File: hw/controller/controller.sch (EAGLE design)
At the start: 102 parts, among them J1 XT30XT30PW_MALE, J2 XT30XT30PW_MALE, M1 MOUNT, M2 MOUNT, M3 MOUNT, M4 MOUNT, Q1 TPH1R204PLSOP_ADVANCE_8, Q2 TPH1R204PLSOP_ADVANCE_8, Q3 TPH1R204PLSOP_ADVANCE_8, Q4 TPH1R204PLSOP_ADVANCE_8, Q5 TPH1R204PLSOP_ADVANCE_8, Q6 TPH1R204PLSOP_ADVANCE_8, U1 STM32G474CEU6, U2 TCAN334G, U3 AS5147, U4 DRV8323RS

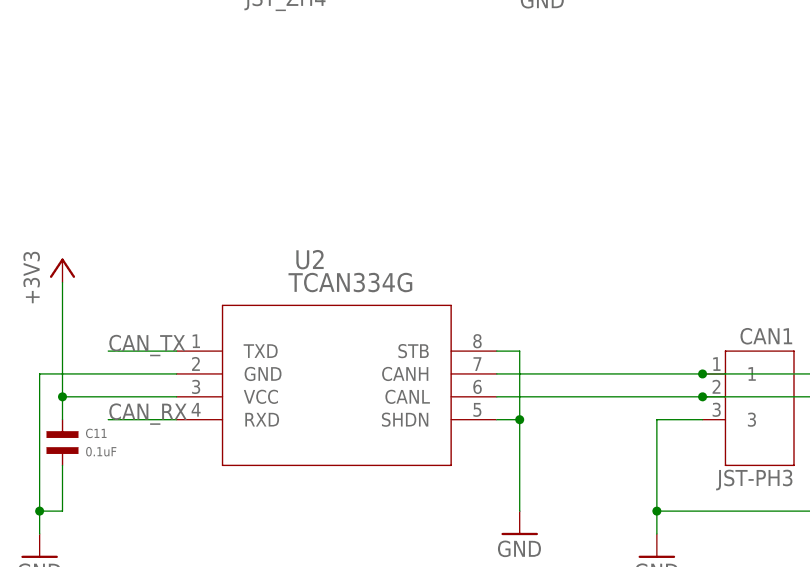
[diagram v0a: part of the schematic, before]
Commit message: Switch to actually using the SOT23-8 variant of the TCAN334G
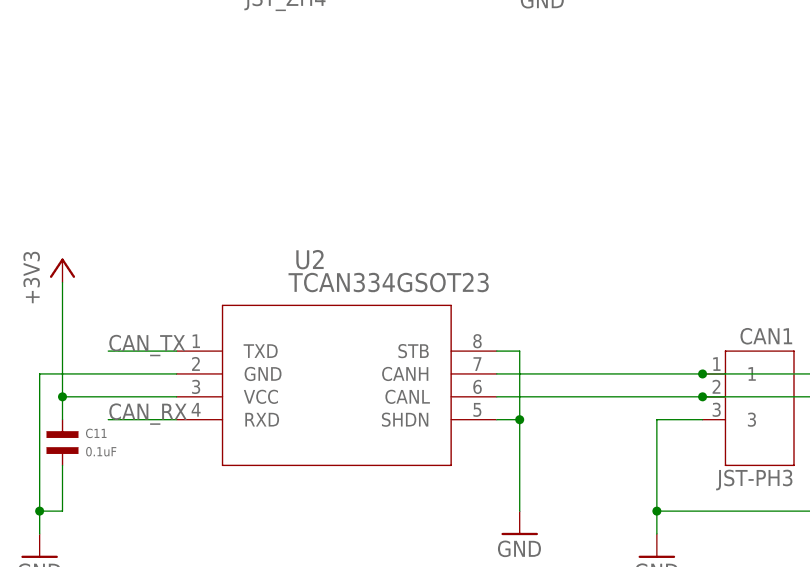
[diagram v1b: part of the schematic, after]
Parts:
- U2: value TCAN334G -> TCAN334GSOT23; device controller:TCAN334G -> controller:TCAN334GSOT23
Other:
- note added: "moteus r4 (c) jjp@pobox.com 2019 Licensed under the Apache 2.0 License"
- note removed: "moteus r4 (c) jjp@pobox.com 2019"
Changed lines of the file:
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@@
 </part>
 <part name="GND6" library="supply1" deviceset="GND" device=""/>
-<part name="U2" library="controller" deviceset="TCAN334G" device="">
+<part name="U2" library="controller" deviceset="TCAN334G" device="SOT23" value="TCAN334GSOT23">
 <attribute name="MF" value="TI"/>
 <attribute name="MPN" value="TCAN334GDCNT"/>
@@
 <text x="-132.08" y="-142.24" size="5.08" layer="90">POWER FETS</text>
 <text x="73.66" y="-142.24" size="5.08" layer="90">BULK CAPACITANCE</text>
-<text x="137.16" y="203.2" size="7.62" layer="90">moteus r4
-(c) jjp@pobox.com
-2019</text>
+<text x="-307.34" y="200.66" size="7.62" layer="90">moteus r4
+(c) jjp@pobox.com 2019
+Licensed under the Apache 2.0 License</text>
 </plain>
 <instances>

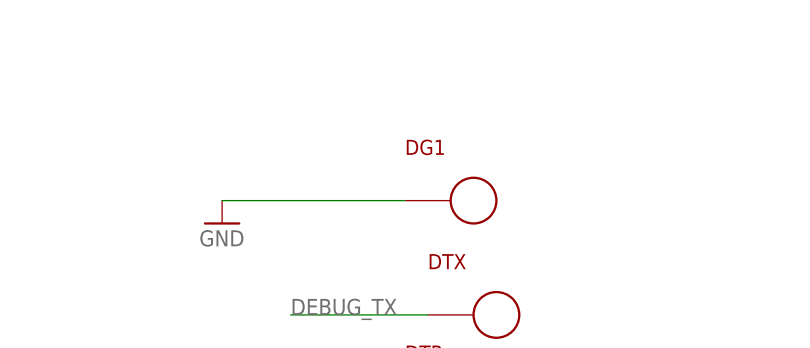
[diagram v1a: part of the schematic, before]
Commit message: Clean up outer boundary and add a 3v3 test point
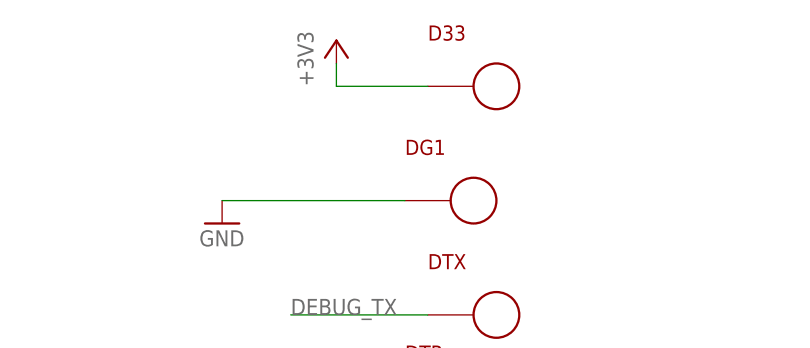
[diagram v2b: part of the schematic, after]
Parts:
- added D33: PAD24AWG_PAD, controller:PAD24AWG_PAD
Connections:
- net +3V3: now also D33.P$1
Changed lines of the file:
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@@
 <part name="GND20" library="supply1" deviceset="GND" device=""/>
 <part name="GND21" library="supply1" deviceset="GND" device=""/>
+<part name="D33" library="controller" deviceset="PAD" device="24AWG_PAD">
+<attribute name="POPULATE" value="0"/>
+</part>
+<part name="+3V13" library="supply1" deviceset="+3V3" device=""/>
 </parts>
 <sheets>
@@
 <instance part="GND20" gate="1" x="144.78" y="170.18"/>
 <instance part="GND21" gate="1" x="149.86" y="38.1"/>
+<instance part="D33" gate="G$1" x="175.26" y="185.42">
+<attribute name="POPULATE" x="175.26" y="185.42" size="7.62" layer="96" display="off"/>
+</instance>
+<instance part="+3V13" gate="G$1" x="157.48" y="190.5"/>
 </instances>
 <busses>
@@
 <wire x1="-236.22" y1="-10.16" x2="-228.6" y2="-10.16" width="0.1524" layer="91"/>
 <junction x="-228.6" y="-10.16"/>
+</segment>
+<segment>
+<pinref part="+3V13" gate="G$1" pin="+3V3"/>
+<wire x1="157.48" y1="187.96" x2="157.48" y2="185.42" width="0.1524" layer="91"/>
+<pinref part="D33" gate="G$1" pin="P$1"/>
+<wire x1="157.48" y1="185.42" x2="167.64" y2="185.42" width="0.1524" layer="91"/>
 </segment>
 </net>
@@
 </sheet>
 </sheets>
-<errors>
-</errors>
 </schematic>
 </drawing>

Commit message: Mark some more things as not populated
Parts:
- DA, DB, DC, TEMP1, TEMP2: POPULATE (none) -> 0
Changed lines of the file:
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@@
 <attribute name="MPN" value="MF-CAP-0402-0.1uF"/>
 </part>
-<part name="TEMP1" library="controller" deviceset="PAD" device="24AWG_PAD"/>
-<part name="TEMP2" library="controller" deviceset="PAD" device="24AWG_PAD"/>
-<part name="DA" library="controller" deviceset="PAD" device="24AWG_PAD"/>
-<part name="DB" library="controller" deviceset="PAD" device="24AWG_PAD"/>
-<part name="DC" library="controller" deviceset="PAD" device="24AWG_PAD"/>
+<part name="TEMP1" library="controller" deviceset="PAD" device="24AWG_PAD">
+<attribute name="POPULATE" value="0"/>
+</part>
+<part name="TEMP2" library="controller" deviceset="PAD" device="24AWG_PAD">
+<attribute name="POPULATE" value="0"/>
+</part>
+<part name="DA" library="controller" deviceset="PAD" device="24AWG_PAD">
+<attribute name="POPULATE" value="0"/>
+</part>
+<part name="DB" library="controller" deviceset="PAD" device="24AWG_PAD">
+<attribute name="POPULATE" value="0"/>
+</part>
+<part name="DC" library="controller" deviceset="PAD" device="24AWG_PAD">
+<attribute name="POPULATE" value="0"/>
+</part>
 <part name="U1" library="controller" deviceset="STM32G474CEU6" device="">
 <attribute name="MPN" value="STM32G474CEU6"/>
@@
 <attribute name="MF" x="238.76" y="-104.14" size="1.778" layer="96" display="off"/>
 </instance>
-<instance part="TEMP1" gate="G$1" x="185.42" y="-15.24"/>
-<instance part="TEMP2" gate="G$1" x="195.58" y="-17.78"/>
-<instance part="DA" gate="G$1" x="-66.04" y="-208.28" rot="R180"/>
-<instance part="DB" gate="G$1" x="-35.56" y="-208.28" rot="R180"/>
-<instance part="DC" gate="G$1" x="-10.16" y="-208.28" rot="R180"/>
+<instance part="TEMP1" gate="G$1" x="185.42" y="-15.24">
+<attribute name="POPULATE" x="185.42" y="-15.24" size="1.778" layer="96" display="off"/>
+</instance>
+<instance part="TEMP2" gate="G$1" x="195.58" y="-17.78">
+<attribute name="POPULATE" x="195.58" y="-17.78" size="1.778" layer="96" display="off"/>
+</instance>
+<instance part="DA" gate="G$1" x="-66.04" y="-208.28" rot="R180">
+<attribute name="POPULATE" x="-66.04" y="-208.28" size="1.778" layer="96" rot="R180" display="off"/>
+</instance>
+<instance part="DB" gate="G$1" x="-35.56" y="-208.28" rot="R180">
+<attribute name="POPULATE" x="-35.56" y="-208.28" size="1.778" layer="96" rot="R180" display="off"/>
+</instance>
+<instance part="DC" gate="G$1" x="-10.16" y="-208.28" rot="R180">
+<attribute name="POPULATE" x="-10.16" y="-208.28" size="1.778" layer="96" rot="R180" display="off"/>
+</instance>
 <instance part="U1" gate="G$1" x="-68.58" y="121.92">
 <attribute name="MPN" x="-68.58" y="121.92" size="7.62" layer="96" display="off"/>

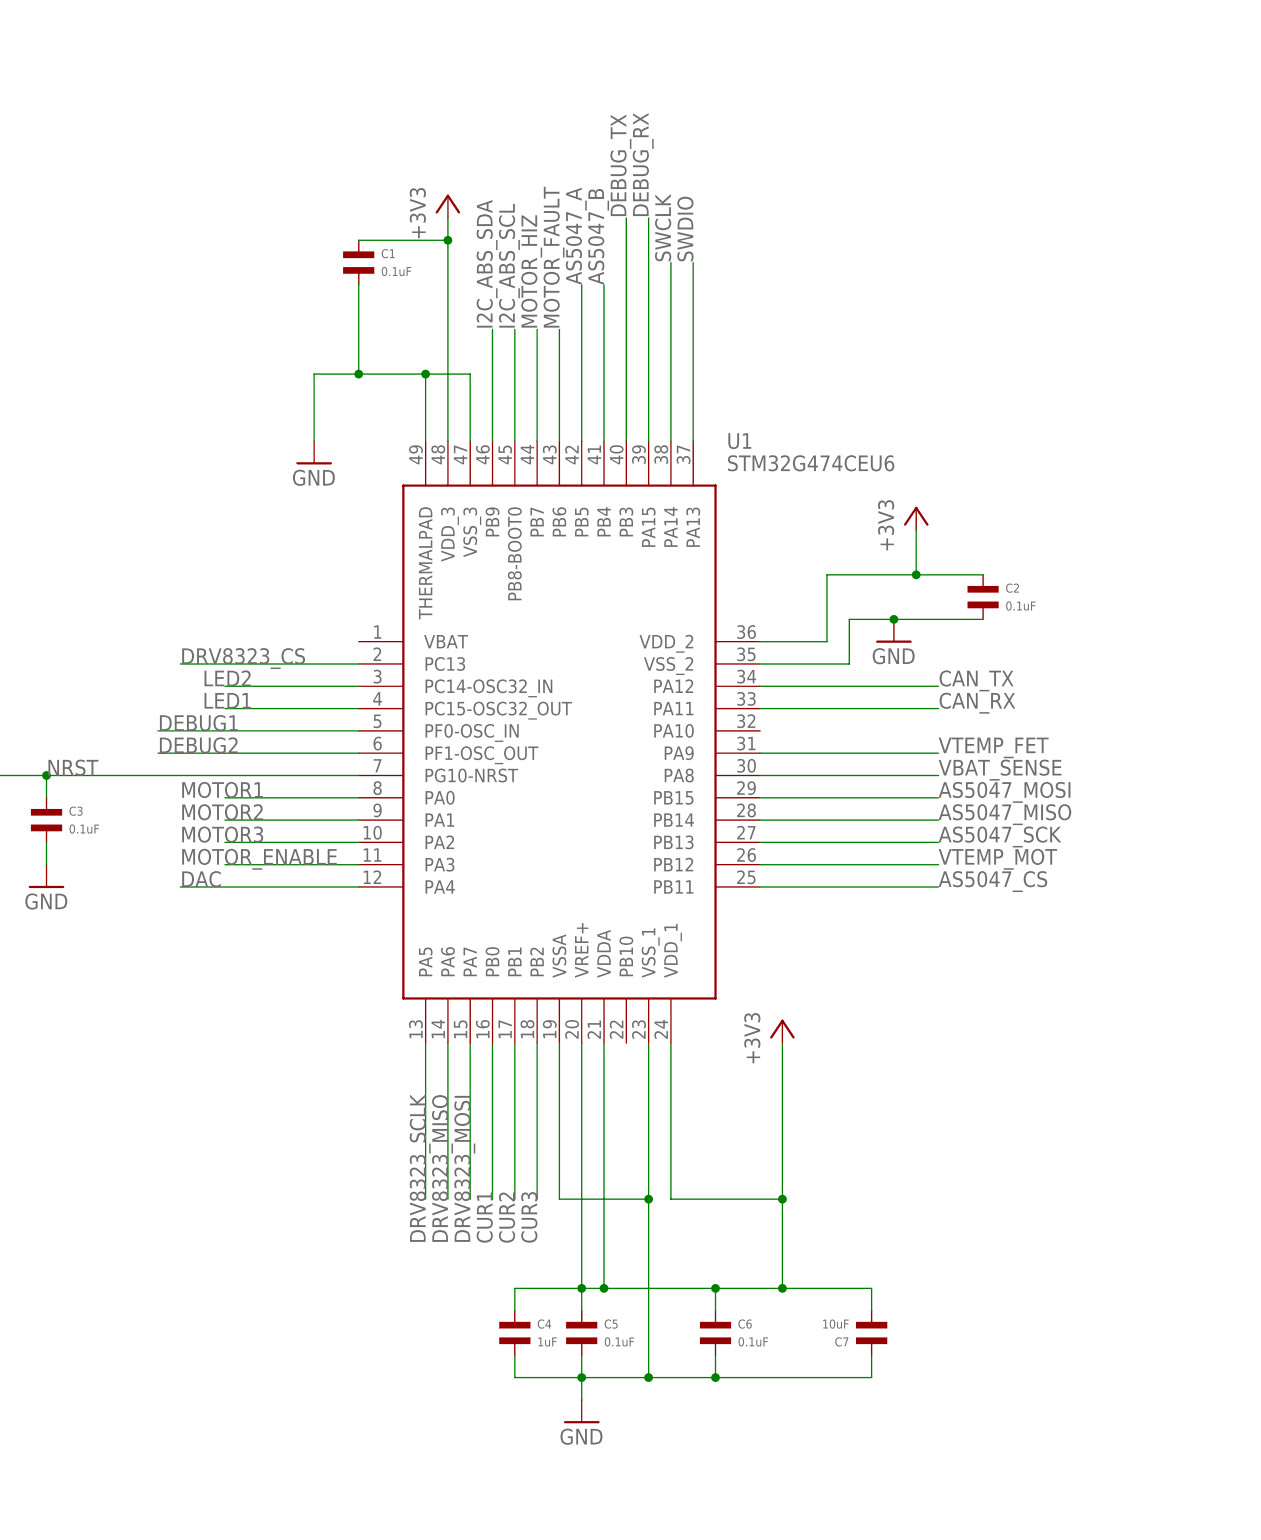
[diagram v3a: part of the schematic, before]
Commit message: controller: Likely finished r4.1 design
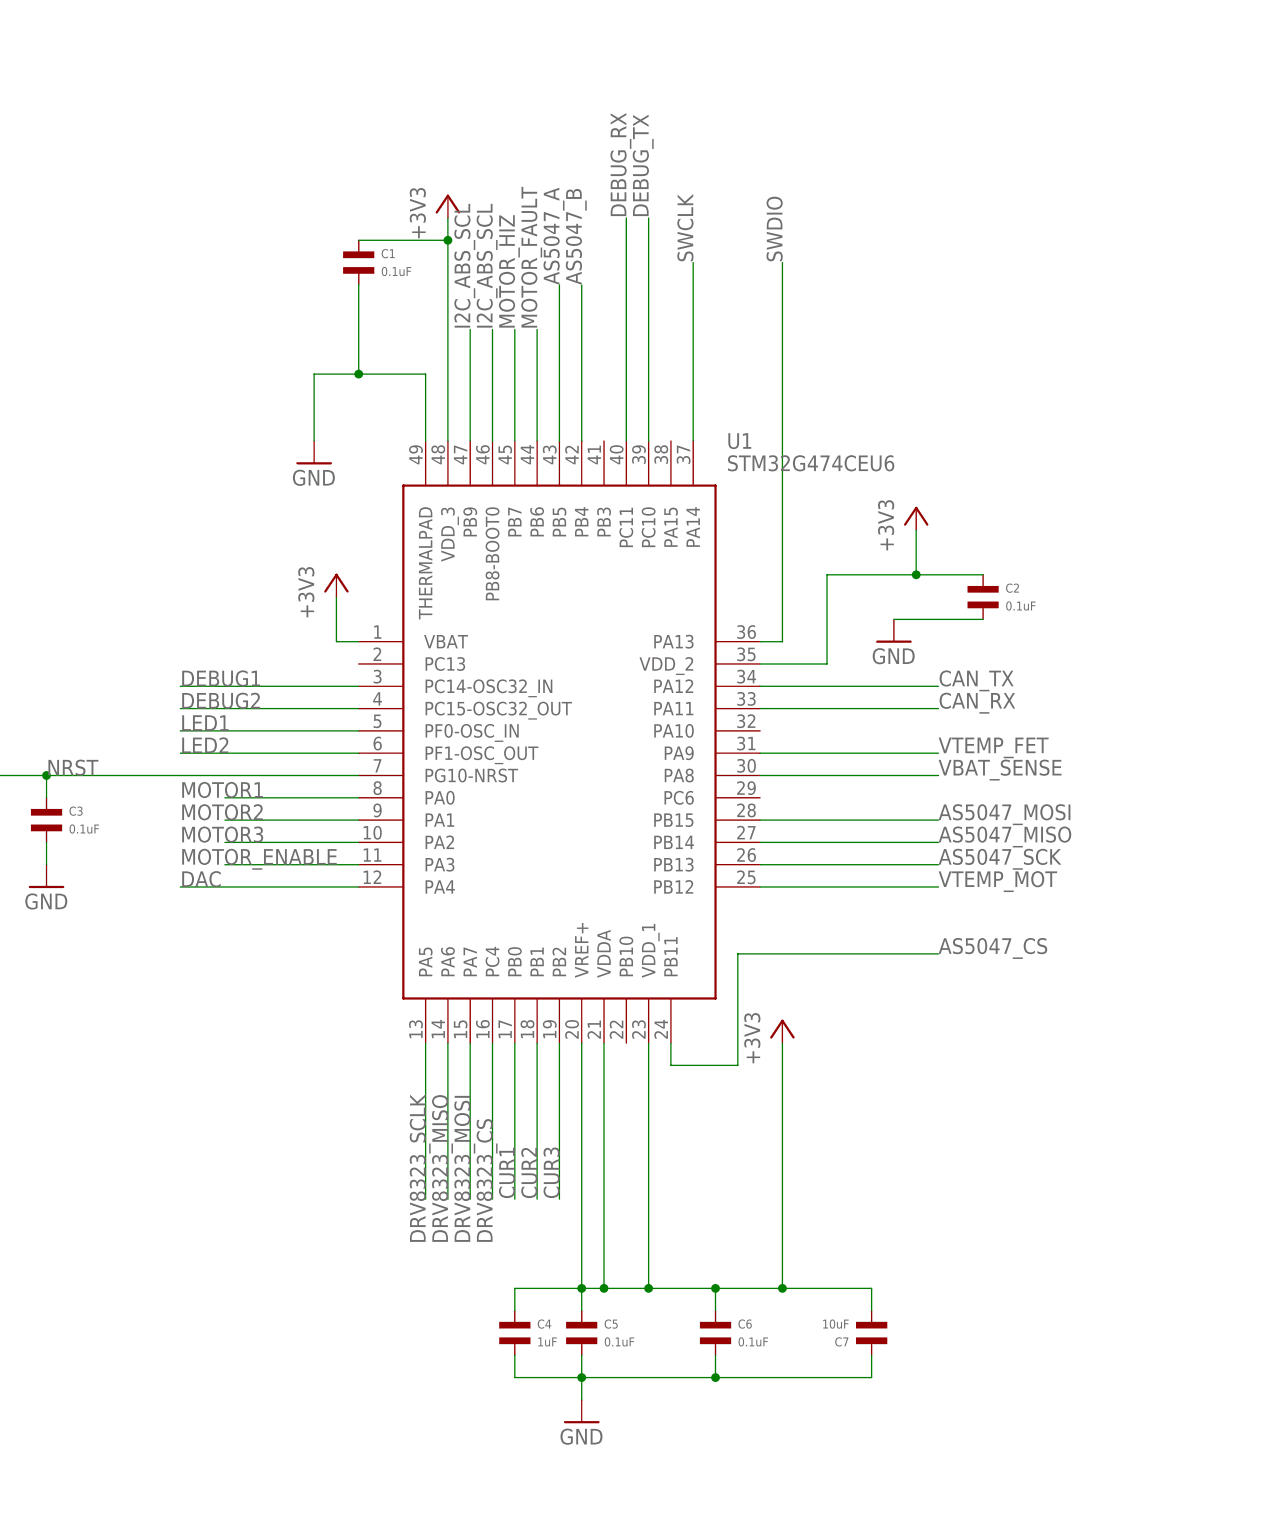
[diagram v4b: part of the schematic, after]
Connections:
- net +3V3: now also U1.VBAT
- net DEBUG1: now also U1.PC14-OSC32_IN; no longer U1.PF0-OSC_IN
- net DEBUG2: now also U1.PC15-OSC32_OUT; no longer U1.PF1-OSC_OUT
- net DEBUG_RX: now also U1.PC11; no longer U1.PA15
- net DEBUG_TX: now also U1.PC10; no longer U1.PB3
- net DRV8323_CS: now also U1.PC4; no longer U1.PC13
- net GND: no longer U1.VSSA, U1.VSS_1, U1.VSS_2, U1.VSS_3
- net I2C_ABS_SCL: now also U1.PB9
- net I2C_ABS_SDA: no longer U1.PB9
- net LED1: now also U1.PF0-OSC_IN; no longer U1.PC15-OSC32_OUT
- net LED2: now also U1.PF1-OSC_OUT; no longer U1.PC14-OSC32_IN
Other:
- note added: "moteus r4.1 (c) jjp@pobox.com 2019 Licensed under the Apache 2.0 License"
- note removed: "moteus r4 (c) jjp@pobox.com 2019 Licensed under the Apache 2.0 License"

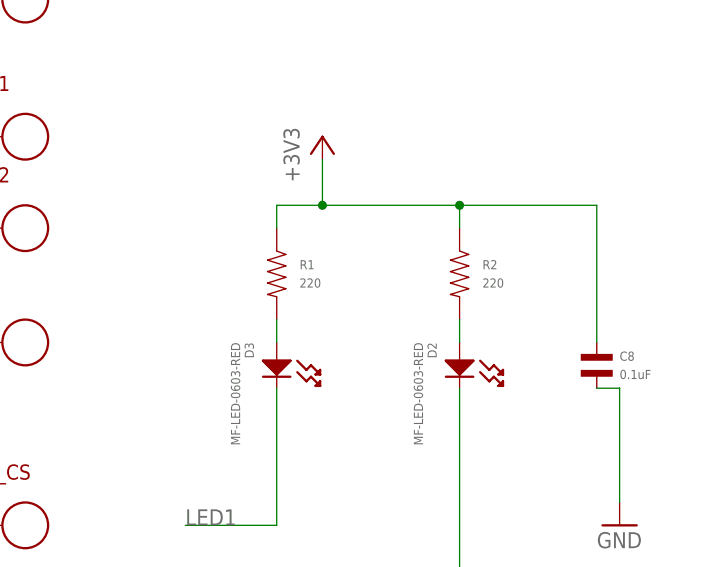
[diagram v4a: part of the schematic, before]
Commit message: controller: Switch LED resistor to 560 ohm
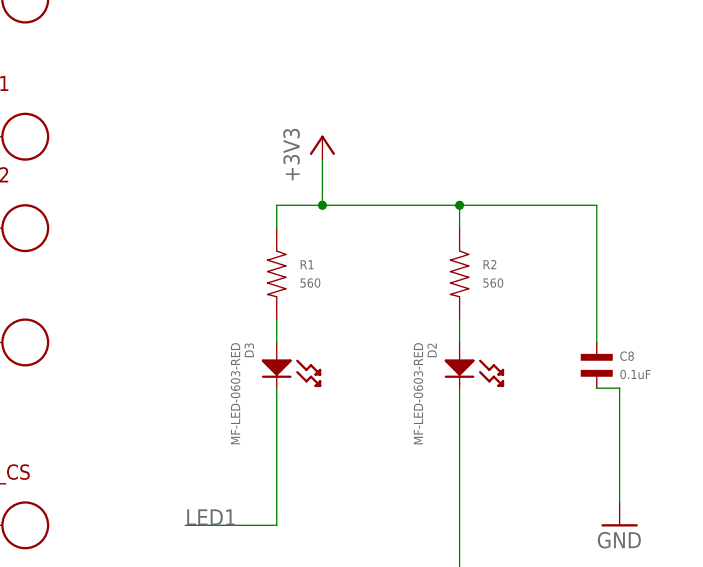
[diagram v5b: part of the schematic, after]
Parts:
- R1, R2: value 220 -> 560; MPN MF-RES-0402-220 -> MF-RES-0402-560
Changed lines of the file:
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@@
 <part name="D3" library="mfleds" deviceset="LED_SINGLE" device="-0603-RED" value="MF-LED-0603-RED"/>
 <part name="+3V7" library="supply1" deviceset="+3V3" device=""/>
-<part name="R1" library="mfpassives" deviceset="RESISTOR" device="_0402" value="220">
+<part name="R1" library="mfpassives" deviceset="RESISTOR" device="_0402" value="560">
 <attribute name="HOUSEPART" value="1"/>
-<attribute name="MPN" value="MF-RES-0402-220"/>
+<attribute name="MPN" value="MF-RES-0402-560"/>
 </part>
-<part name="R2" library="mfpassives" deviceset="RESISTOR" device="_0402" value="220">
+<part name="R2" library="mfpassives" deviceset="RESISTOR" device="_0402" value="560">
 <attribute name="HOUSEPART" value="1"/>
-<attribute name="MPN" value="MF-RES-0402-220"/>
+<attribute name="MPN" value="MF-RES-0402-560"/>
 </part>
 <part name="P+4" library="supply1" deviceset="V+" device=""/>

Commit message: controller: Actually use a 2k resistor for I2C pullup
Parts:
- R3, R4: HOUSEPART (none) -> YES; MF Panasonic -> (none); MPN ERJ-2RKF1002X -> MF-RES-0402-2K
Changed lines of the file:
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@@
 </part>
 <part name="R3" library="mfpassives" deviceset="RESISTOR" device="_0402" value="2k">
-<attribute name="MF" value="Panasonic"/>
-<attribute name="MPN" value="ERJ-2RKF1002X"/>
+<attribute name="HOUSEPART" value="YES"/>
+<attribute name="MF" value=""/>
+<attribute name="MPN" value="MF-RES-0402-2K"/>
 </part>
 <part name="R4" library="mfpassives" deviceset="RESISTOR" device="_0402" value="2k">
-<attribute name="MF" value="Panasonic"/>
-<attribute name="MPN" value="ERJ-2RKF1002X"/>
+<attribute name="HOUSEPART" value="YES"/>
+<attribute name="MF" value=""/>
+<attribute name="MPN" value="MF-RES-0402-2K"/>
 </part>
 <part name="C22" library="mfpassives" deviceset="CAPACITOR_NP" device="_1206" value="10uF">
